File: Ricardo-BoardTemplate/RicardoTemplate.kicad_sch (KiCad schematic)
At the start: 37 parts, among them J1 RBUS, U1 ESP32-S3, U5 LTC4411

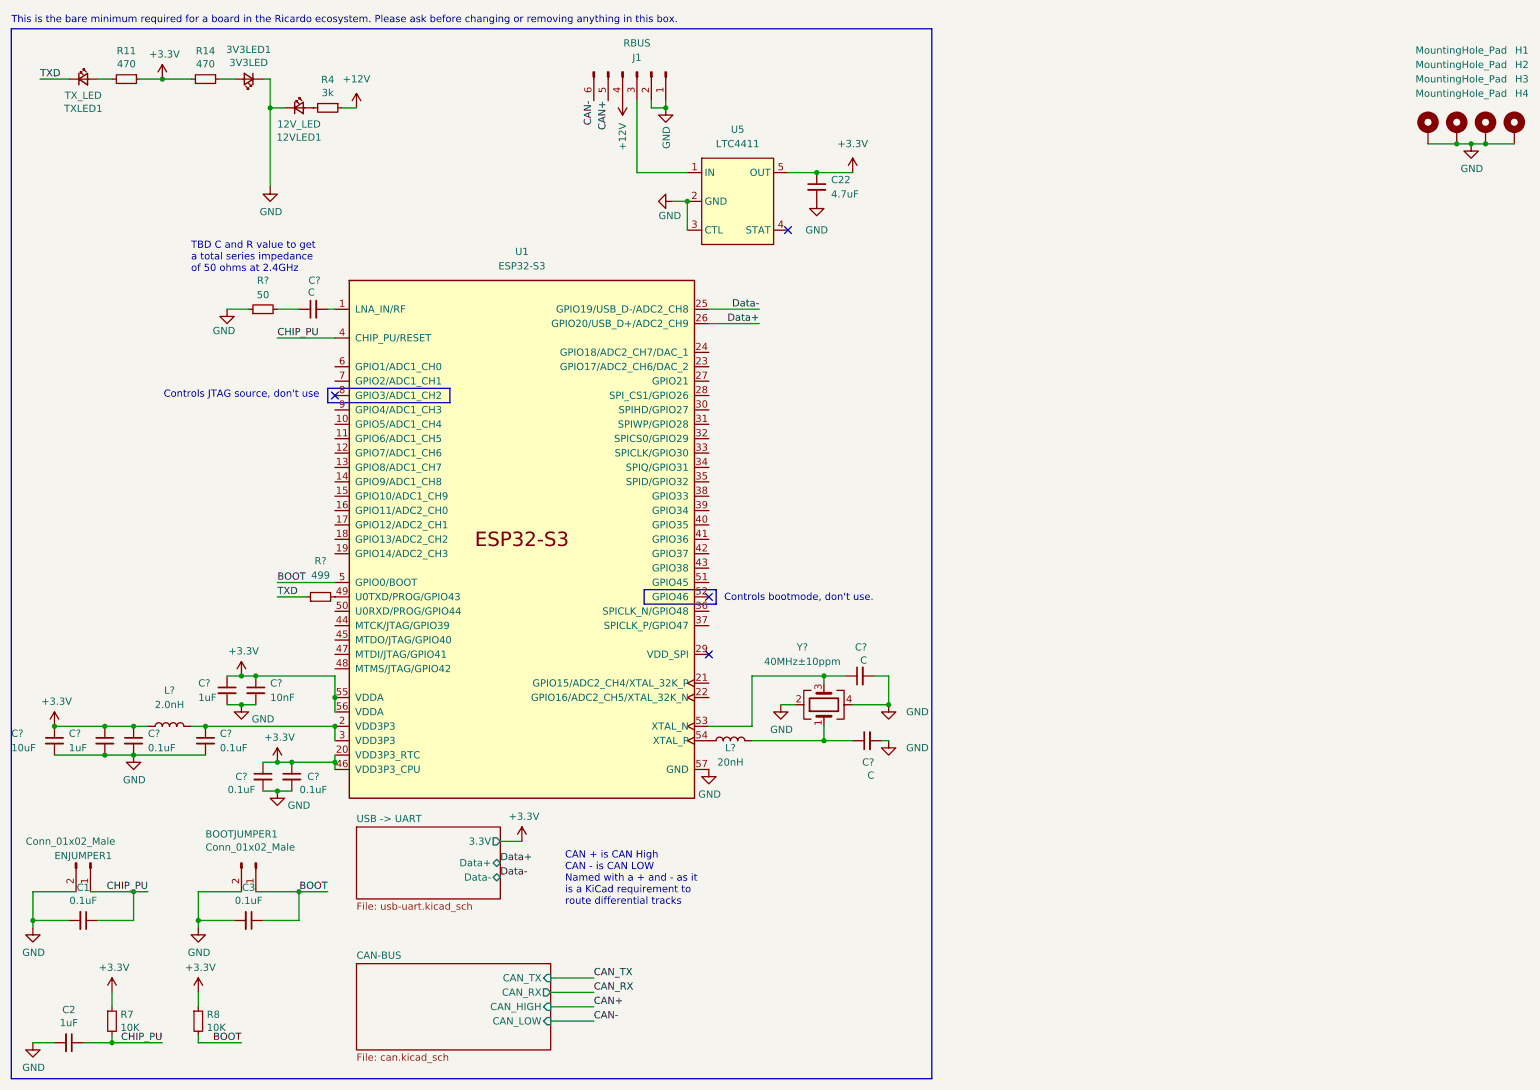
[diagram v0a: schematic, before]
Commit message: most FP assignments to 0402
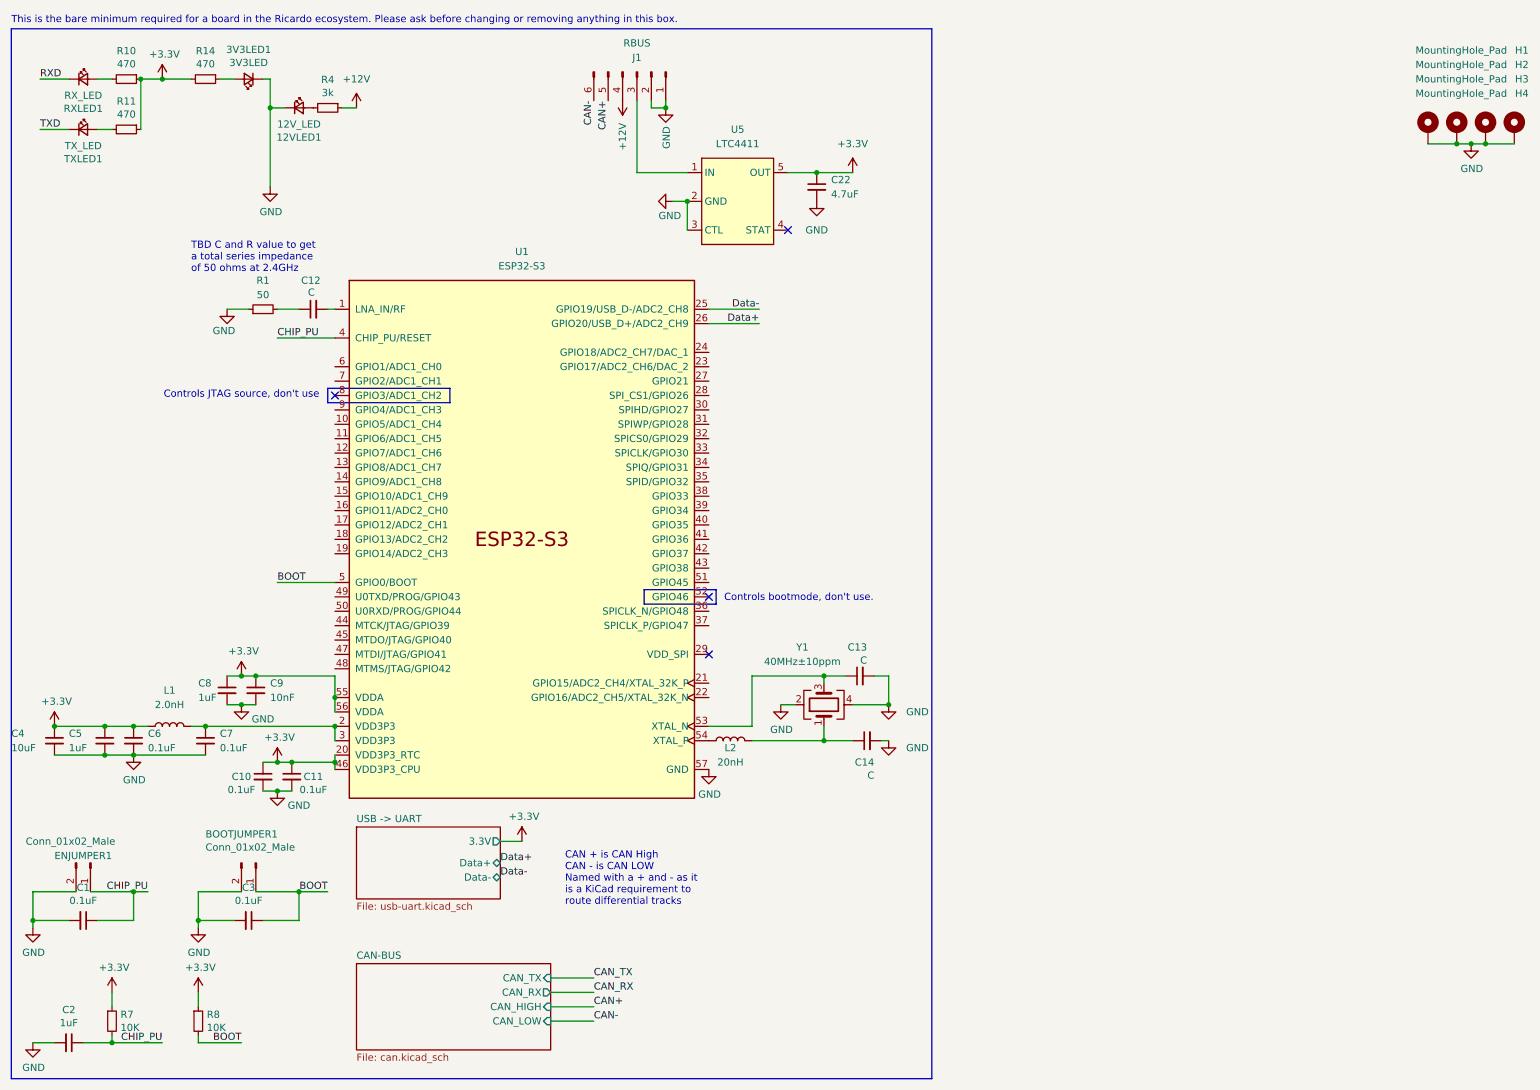
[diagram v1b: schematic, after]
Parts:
- removed R?: 499, symbol Device:R_Small
- added R10: 470, Resistor_SMD:R_0402_1005Metric, symbol Device:R_Small
- added RXLED1: RX_LED, LED_SMD:LED_0603_1608Metric, symbol Device:LED_Small
- 12VLED1, 3V3LED1, TXLED1: footprint LED_SMD:LED_0603_1608Metric -> Resistor_SMD:R_0402_1005Metric
- C1, C2, C3: footprint Capacitor_SMD:C_0603_1608Metric -> Capacitor_SMD:C_0402_1005Metric
- C10, C11: renamed from C?; footprint Capacitor_SMD:C_0603_1608Metric -> Capacitor_SMD:C_0402_1005Metric
- C5, C6, C7, C8, C9: renamed from C?; footprint (none) -> Capacitor_SMD:C_0402_1005Metric
- R11, R14, R4, R7, R8: footprint Resistor_SMD:R_0603_1608Metric -> Resistor_SMD:R_0402_1005Metric
- Y1: renamed from Y?; footprint (none) -> Crystal:Crystal_SMD_2016-4Pin_2.0x1.6mm
- gave numbers to parts that had none: 7
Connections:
- net +3V3: now also R10.1
- new net: R10.2, RXLED1.2 (A)
- new net RXD: RXLED1.1 (K)
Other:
- moved on the sheet: R11, TXLED1

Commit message: Initial buck boost layout
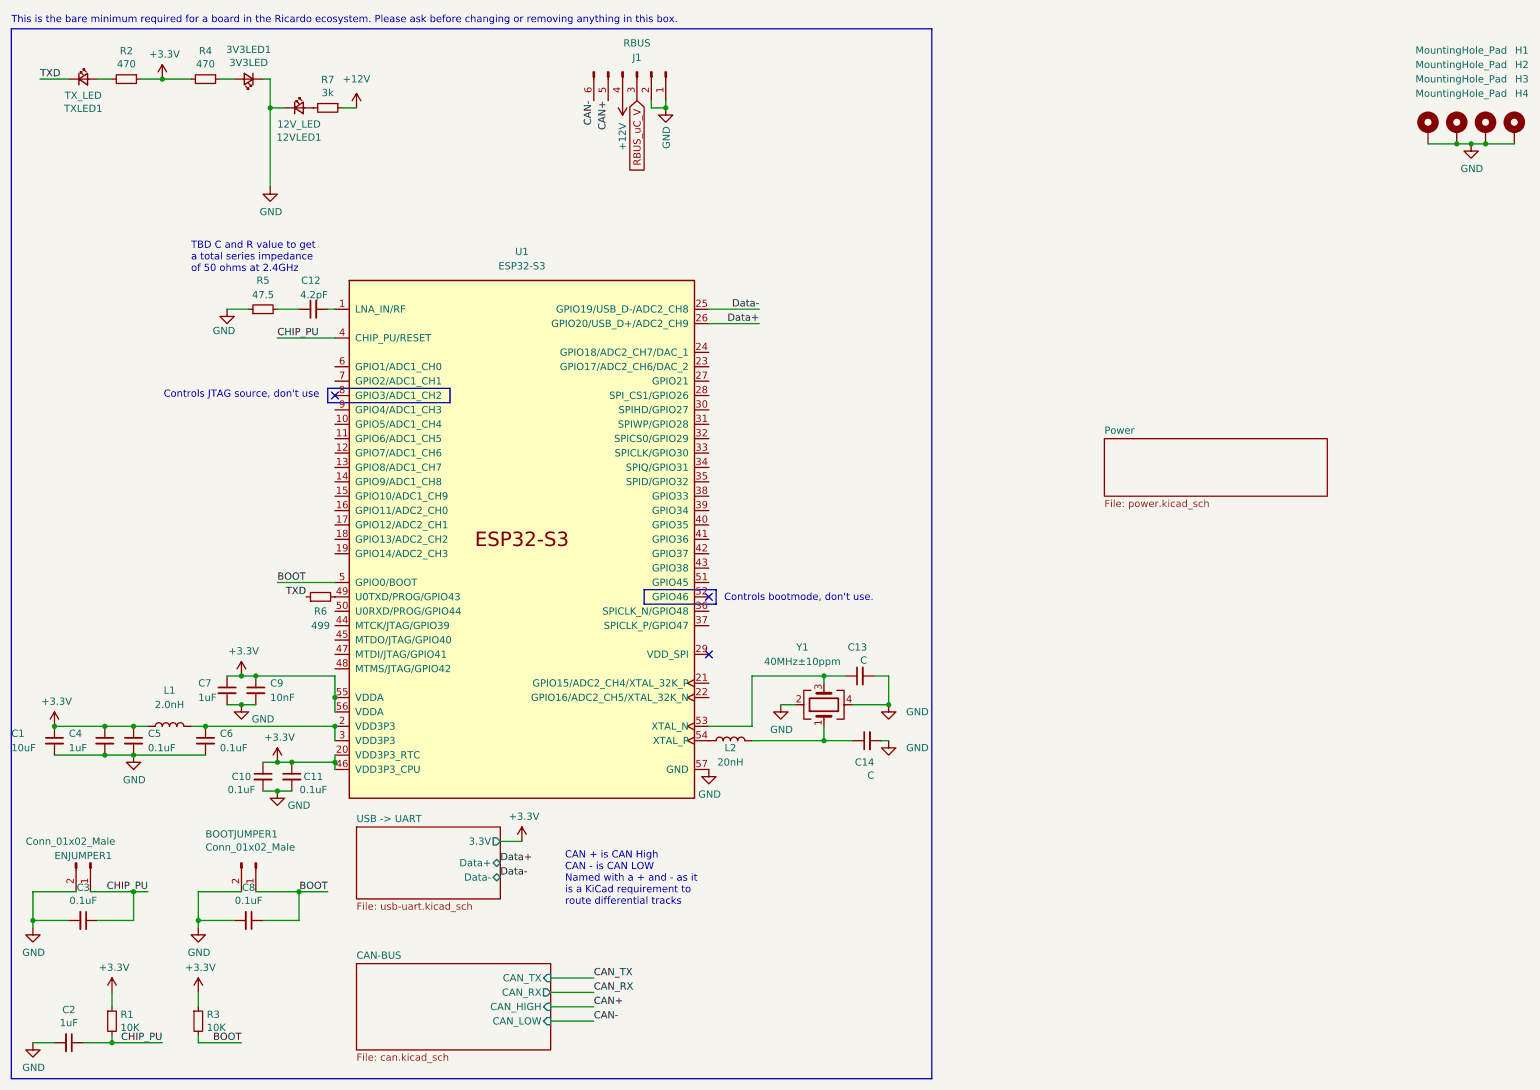
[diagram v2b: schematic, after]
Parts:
- removed C22: 4.7uF, Capacitor_SMD:C_0603_1608Metric, symbol Device:C_Small
- removed R10: 470, Resistor_SMD:R_0402_1005Metric, symbol Device:R_Small
- removed RXLED1: RX_LED, LED_SMD:LED_0603_1608Metric, symbol Device:LED_Small
- removed U5: LTC4411, Package_TO_SOT_SMD:SOT-23-5, symbol iclr:LTC4411
- added R6: 499, Resistor_SMD:R_0402_1005Metric, symbol Device:R_Small
- C1: renamed from C4; footprint (none) -> Capacitor_SMD:C_0402_1005Metric
- C12: value C -> 4.2pF; footprint Capacitor_SMD:C_0603_1608Metric -> Capacitor_SMD:C_0402_1005Metric
- C13, C14: footprint Capacitor_SMD:C_0603_1608Metric -> Capacitor_SMD:C_0402_1005Metric
- L1, L2: footprint (none) -> Inductor_SMD:L_0402_1005Metric
- R5: renamed from R1; value 50 -> 47.5; footprint (none) -> Resistor_SMD:R_0402_1005Metric
- renumbered C1 to C3, C5 to C4, C6 to C5, C7 to C6, C8 to C7, C3 to C8, R7 to R1, R11 to R2, R8 to R3, R14 to R4, R4 to R7
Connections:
- net TXD: now also R6.1
- net RBUS_uC_V: now reaches J1.3 (Pin_3)
- net at U1.49 (U0TXD/PROG/GPIO43): now also R6.2
- no-connect marks 4 -> 3
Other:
- added sheet Power (power.kicad_sch)
- moved on the sheet: R2, TXLED1
